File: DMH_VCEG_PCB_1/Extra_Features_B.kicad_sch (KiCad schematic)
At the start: 35 parts, among them Q8 BC548, SW2 SW_DPDT_x2, U10 TL074, U12 40106, U13 CD4066BE, U17 TL074

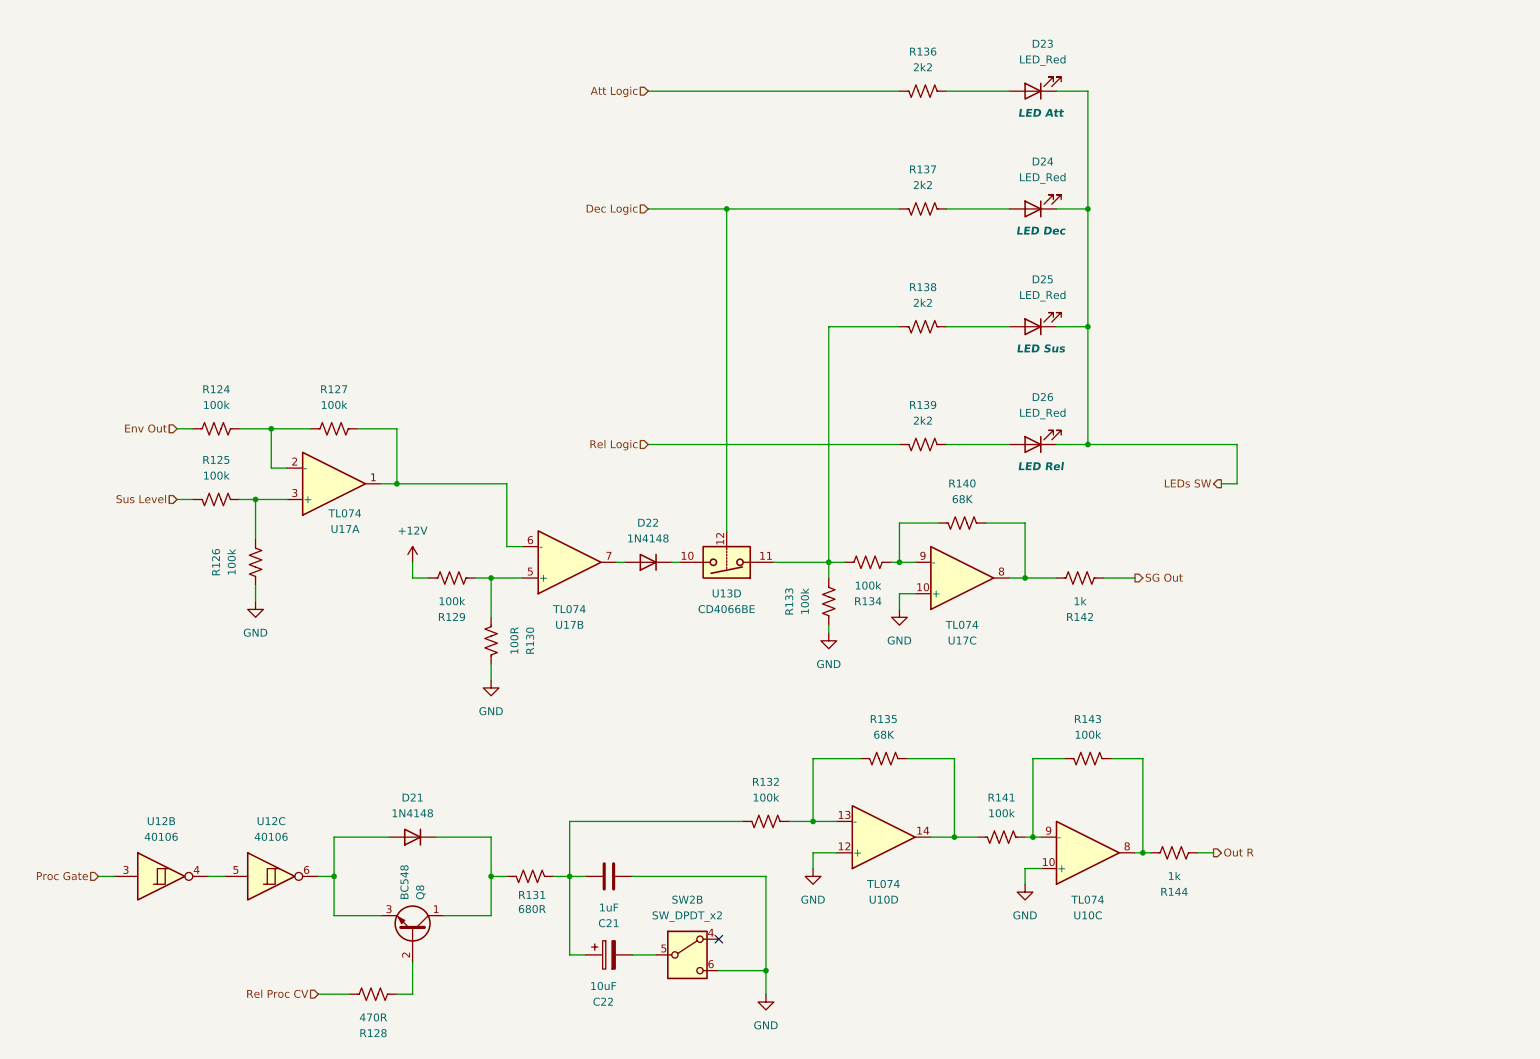
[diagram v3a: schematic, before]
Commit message: Updated SG Out circuit
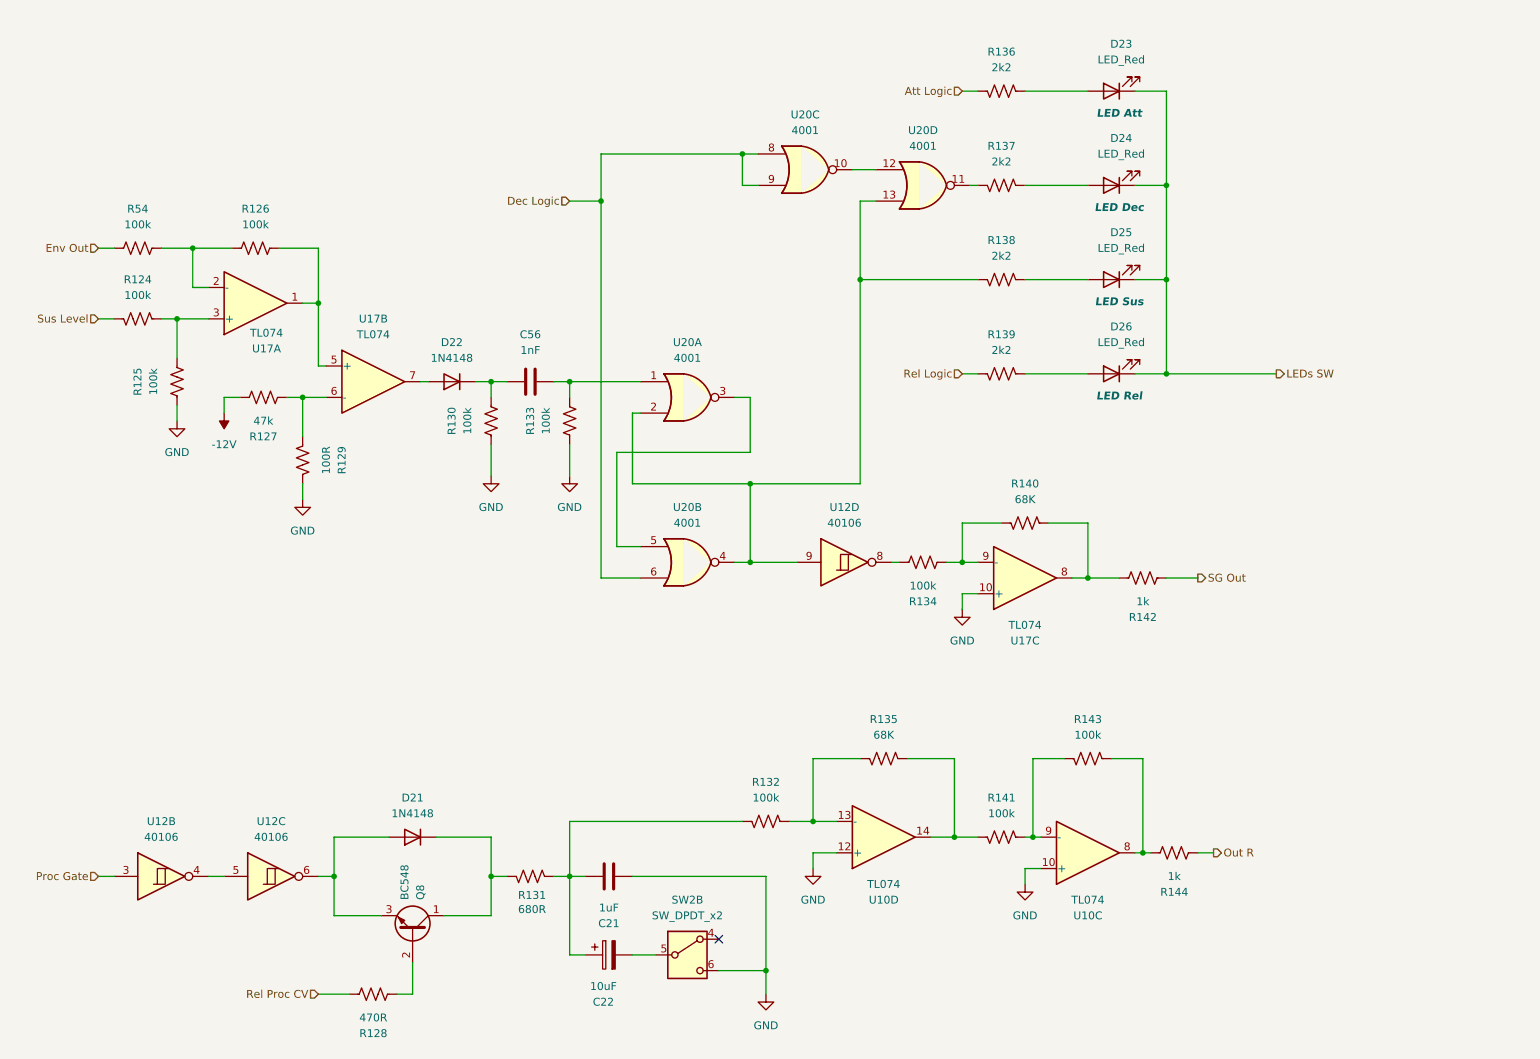
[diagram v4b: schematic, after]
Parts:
- removed U13: CD4066BE, Package_DIP:DIP-14_W7.62mm, symbol Analog_Switch:CD4066BE
- added C56: 1nF, Capacitor_THT:C_Disc_D4.3mm_W1.9mm_P5.00mm, symbol Device:C
- added R54: 100k, Resistor_THT:R_Axial_DIN0207_L6.3mm_D2.5mm_P7.62mm_Horizontal, symbol Device:R_US
- added unit 4 of U12
- added U20: 4001, symbol 4xxx:4001
- R127: value 100k -> 47k
- R129: value 100k -> 100R
- R130: value 100R -> 100k
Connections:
- net Dec Logic: now also U20.6, U20.8, U20.9; no longer R137.1
- net Env Out: now also R54.2; no longer R124.2
- net GND: now also R125.2, R129.2; no longer R126.2
- net Sus Level: now also R124.1; no longer R125.1
- net at D22.1 (K): now also R130.1, C56.1
- net +12V: no longer names the net of R129.1
- net +12V: now also R127.2, U17.6 (-)
- new net: R134.1, U12.8
- new net: R138.1, U12.9, U20.13, U20.2, U20.4
- new net: R124.2, R125.1, U17.3 (+)
- new net: R137.1, U20.11
- new net: U20.10, U20.12
- new net: R126.1, U17.1, U17.5 (+)
- new net: R126.2, R54.1, U17.2 (-)
- new net: C56.2, R133.1, U20.1
- new net: U20.3, U20.5
- new net -12V: R127.1

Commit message: Added Loop circuit
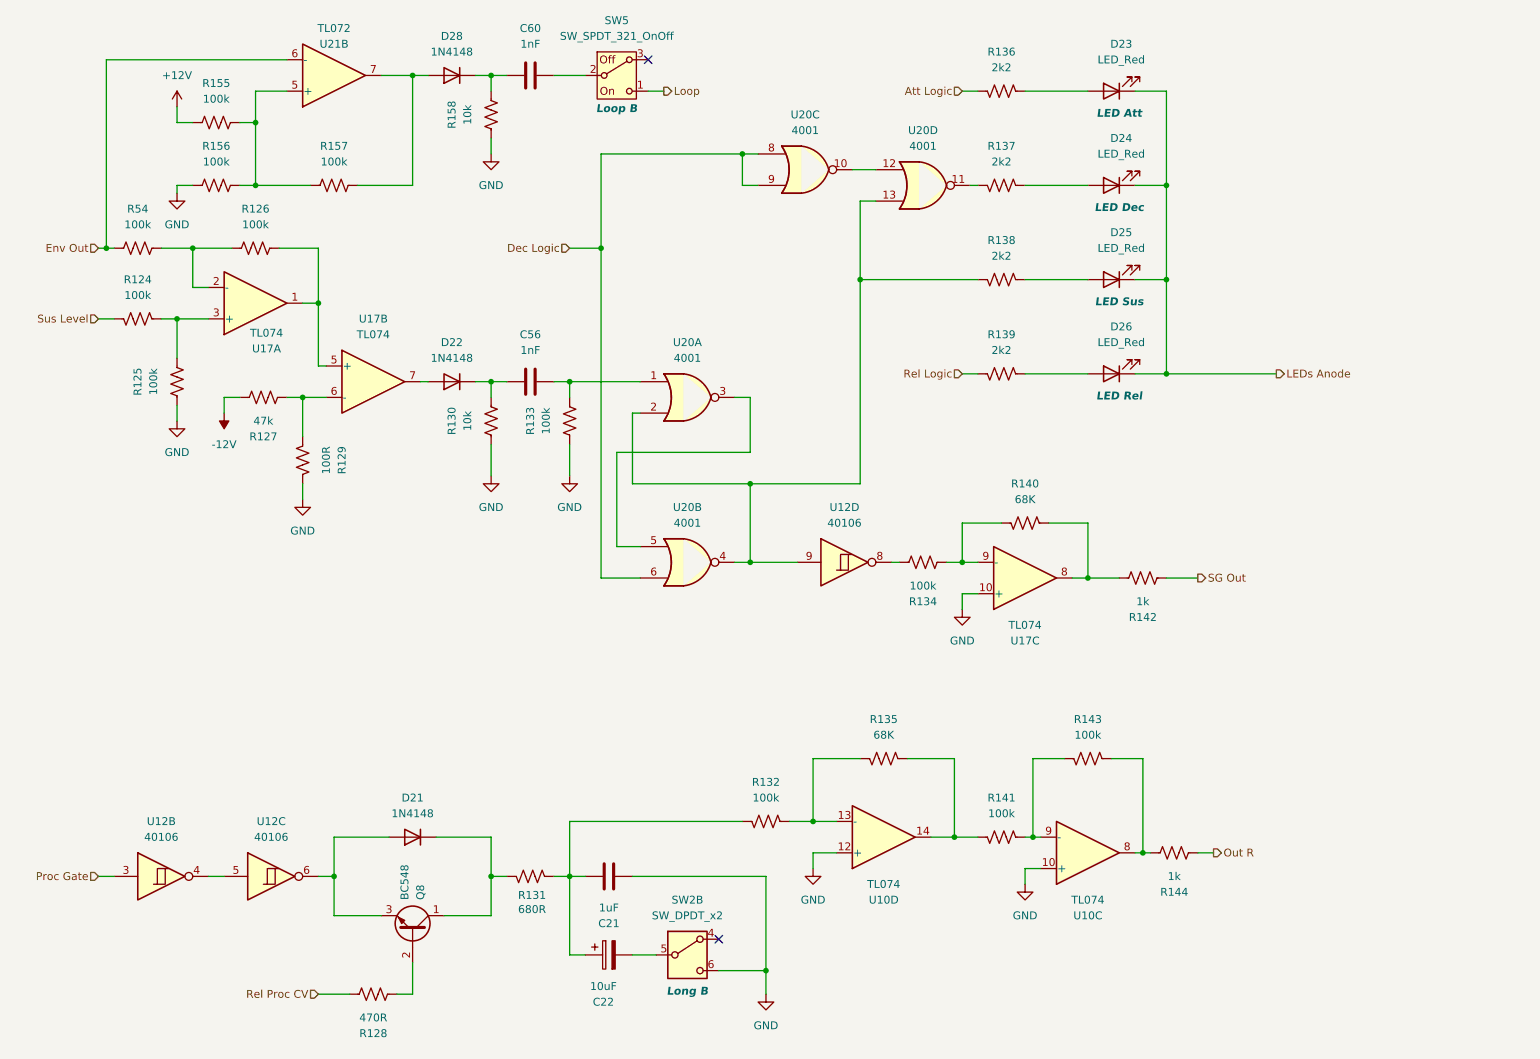
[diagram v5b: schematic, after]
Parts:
- added C60: 1nF, Capacitor_THT:C_Disc_D4.3mm_W1.9mm_P5.00mm, symbol Device:C
- added D28: 1N4148, Diode_THT:D_DO-35_SOD27_P7.62mm_Horizontal, symbol Diode:1N4148
- added R155, R156, R157: 100k, Resistor_THT:R_Axial_DIN0207_L6.3mm_D2.5mm_P7.62mm_Horizontal, symbol Device:R_US
- added R158: 10k, Resistor_THT:R_Axial_DIN0207_L6.3mm_D2.5mm_P7.62mm_Horizontal, symbol Device:R_US
- added SW5: SW_SPDT_321_OnOff, SynthStuff:Toggle_Switch_TE, symbol SynthStuff:SW_SPDT_321_OnOff
- added U21: TL072, Package_DIP:DIP-8_W7.62mm, symbol Amplifier_Operational:TL072
- R130: value 100k -> 10k
- SW2: Function (none) -> Long B
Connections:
- net Env Out: now also U21.6 (-)
- net GND: now also R156.2, R158.2
- net LEDs SW renamed LEDs Anode
- new net: C60.1, D28.1 (K), R158.1
- new net: D28.2 (A), R157.1, U21.7
- new net: R155.1, R156.1, R157.2, U21.5 (+)
- new net: C60.2, SW5.2 (B)
- new net +12V: R155.2
- new net Loop: SW5.1 (C)
- no-connect marks 1 -> 2

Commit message: PCB 1 ready for placement
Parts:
- removed U21: TL072, Package_DIP:DIP-8_W7.62mm, symbol Amplifier_Operational:TL072
- added J25, J26: Conn_01x10_PinHeader, symbol SynthStuff:Conn_01x10_PinHeader
- added unit 4 of U17
- U20: footprint (none) -> Package_DIP:DIP-14_W7.62mm_Socket
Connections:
- net Att Logic: now also J25.8 (Pin_8)
- net Dec Logic: now also J25.9 (Pin_9)
- net Env Out: now also U17.13 (-)
- net Loop: now also J26.3 (Pin_3)
- net Proc Gate: now also J26.4 (Pin_4)
- net Rel Logic: now also J25.10 (Pin_10)
- net Rel Proc CV: now also J26.6 (Pin_6)
- net SG Out: now also J26.9 (Pin_9)
- net Sus Level: now also J26.10 (Pin_10)
- net at R134.1, U12.8: now also J26.7 (Pin_7)
- net at R138.1, U12.9, U20.13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: now also J26.8 (Pin_8)
- net at D21.2 (A), Q8.3 (E), U12.6: now also J26.5 (Pin_5)
- net at D28.2 (A), R157.1: now also U17.14
- net at R155.1, R156.1, R157.2: now also U17.12 (+)
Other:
- note added: "PCB 1"
- moved on the sheet: C21, C22, D21, Q8, R128, R131, R132, R134, R135, R140, R141, R142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

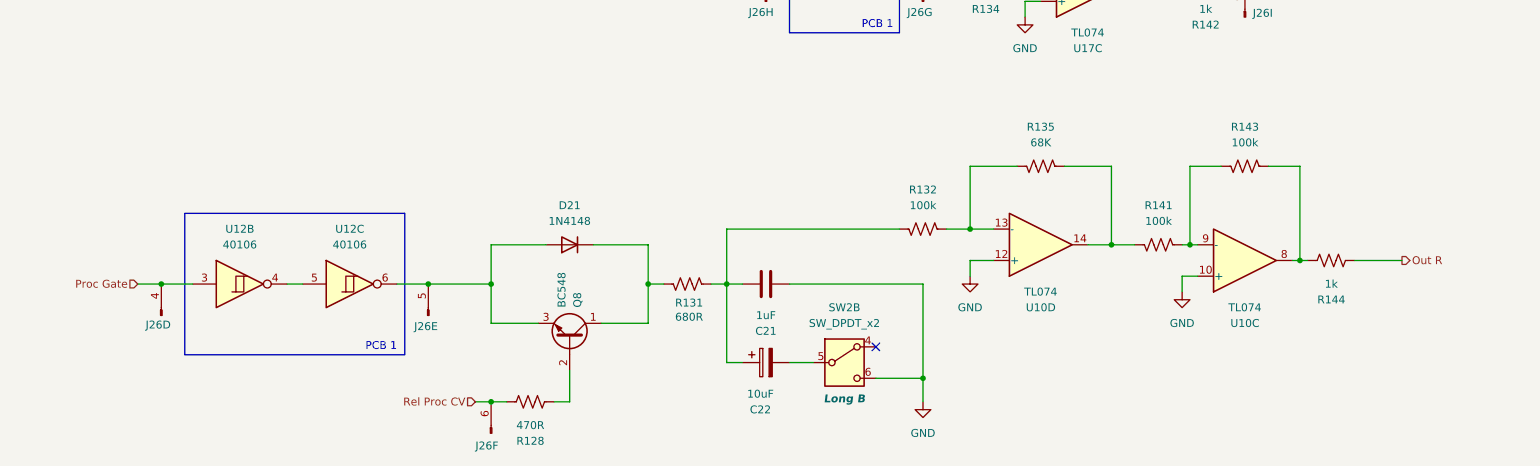
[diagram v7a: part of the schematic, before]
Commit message: Placed ICs and pin headers on PCB 2
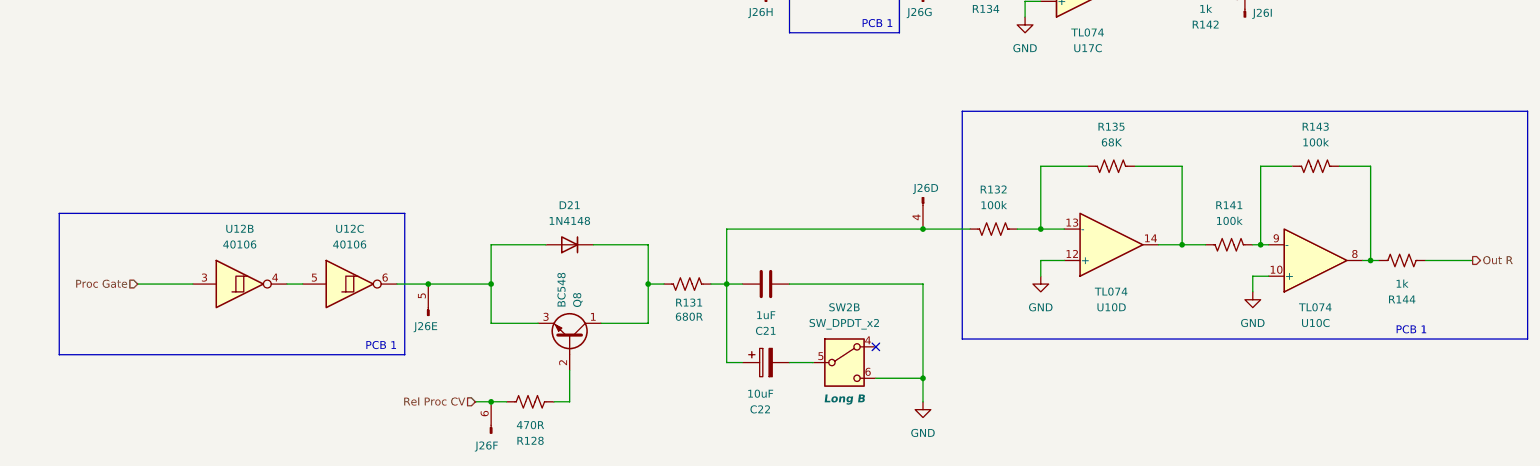
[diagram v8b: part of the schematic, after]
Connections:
- net Proc Gate: no longer J26.4 (Pin_4)
- net at C21.1, C22.1, R131.1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: now also J26.4 (Pin_4)
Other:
- moved on the sheet: R132, R135, R141, R143, R144, U10C, U10D
